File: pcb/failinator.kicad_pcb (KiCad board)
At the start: 2 copper layers, 200 x 124 mm, 82 parts, among them P1 CONN_01X04, P2 CONN_01X06, P3 CONN_01X06, P4 CONN_01X06, U1 74HC594, U2 RASPIPLUSHEADER, U3 LDS-CD16RI, U4 LDS-CD16RI, U5 74HC594

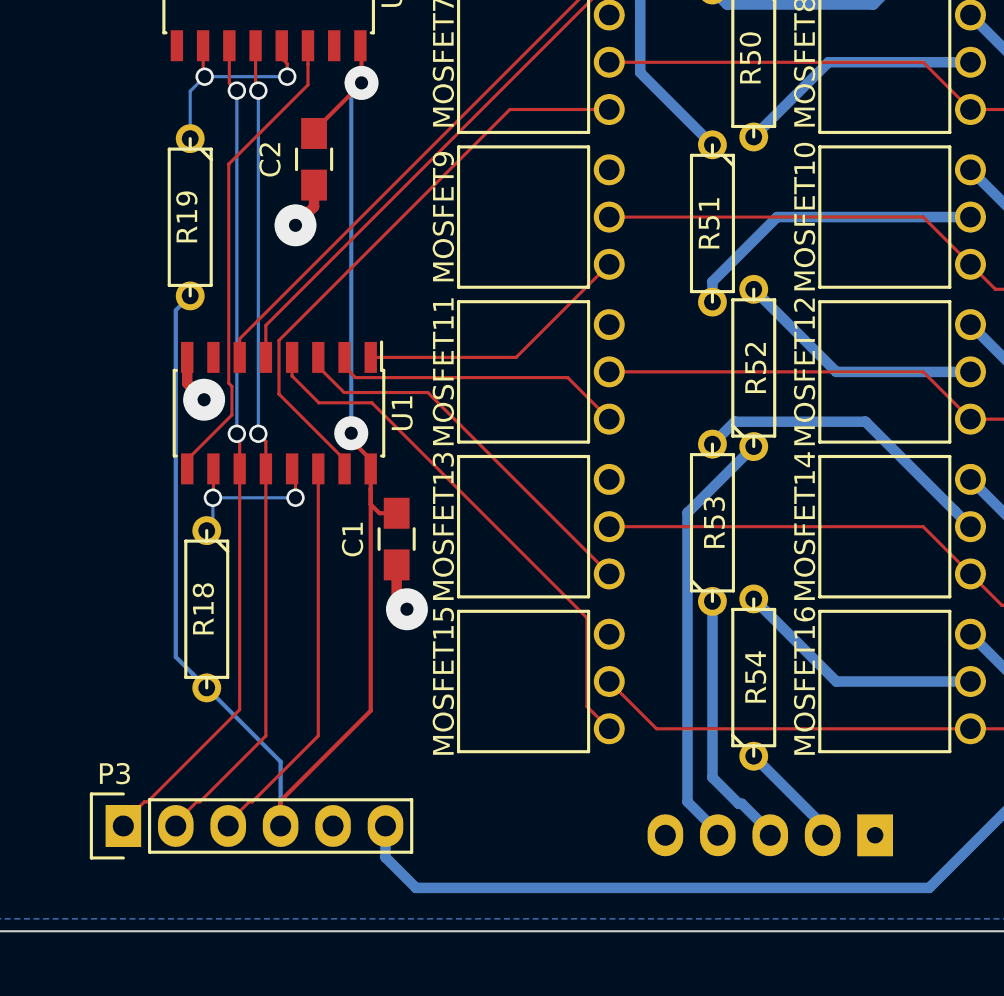
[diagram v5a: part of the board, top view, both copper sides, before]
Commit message: Place some grounds better so they are in the main copper pour
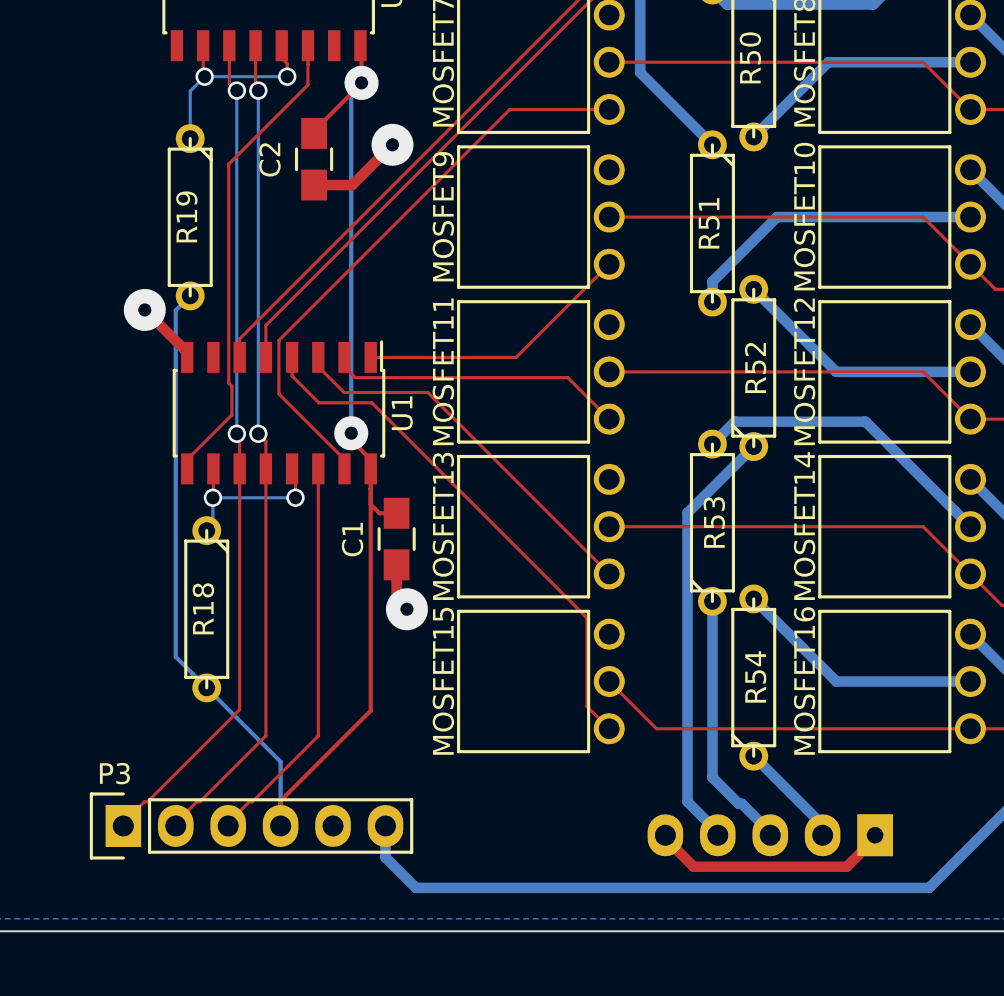
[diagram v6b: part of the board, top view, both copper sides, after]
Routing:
- net /DisplayDrivers/GND: track 9.09 -> 23.7 mm
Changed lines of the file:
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@@
     (thickness 1.6)
     (drawings 16)
-    (tracks 372)
+    (tracks 376)
     (zones 0)
     (modules 82)
@@
   (segment (start 125.5 96.5) (end 125.5 118.75) (width 0.508) (layer F.Cu) (net 37) (status 10))
   (segment (start 125.5 118.75) (end 124.25 120) (width 0.508) (layer F.Cu) (net 37) (status 20))
-  (segment (start 249.7 33.45) (end 249.7 34.5) (width 0.508) (layer F.Cu) (net 38))
-  (segment (start 249.7 34.5) (end 248.8 35.4) (width 0.508) (layer F.Cu) (net 38))
-  (via (at 248.8 35.4) (size 2.032) (drill 0.635) (layers F.Cu B.Cu) (net 38))
+  (segment (start 276.88 64.95) (end 276.88 65.1024) (width 0.508) (layer F.Cu) (net 38))
+  (segment (start 276.88 65.1024) (end 275.50839 66.47401) (width 0.508) (layer F.Cu) (net 38))
+  (segment (start 268.09161 66.47401) (end 266.72 65.1024) (width 0.508) (layer F.Cu) (net 38))
+  (segment (start 275.50839 66.47401) (end 268.09161 66.47401) (width 0.508) (layer F.Cu) (net 38))
+  (segment (start 266.72 65.1024) (end 266.72 64.95) (width 0.508) (layer F.Cu) (net 38))
+  (segment (start 249.7 33.45) (end 251.55 33.45) (width 0.508) (layer F.Cu) (net 38))
+  (segment (start 251.55 33.45) (end 253.5 31.5) (width 0.508) (layer F.Cu) (net 38))
+  (via (at 253.5 31.5) (size 2.032) (drill 0.635) (layers F.Cu B.Cu) (net 38))
+  (segment (start 243.555 41.8) (end 243.555 41.555) (width 0.508) (layer F.Cu) (net 38))
+  (segment (start 243.555 41.555) (end 241.5 39.5) (width 0.508) (layer F.Cu) (net 38))
+  (via (at 241.5 39.5) (size 2.032) (drill 0.635) (layers F.Cu B.Cu) (net 38))
   (segment (start 253.7 51.85) (end 253.7 53.5) (width 0.508) (layer F.Cu) (net 38))
   (segment (start 253.7 53.5) (end 254.2 54) (width 0.508) (layer F.Cu) (net 38))
   (via (at 254.2 54) (size 2.032) (drill 0.635) (layers F.Cu B.Cu) (net 38))
-  (segment (start 244.346901 43.849901) (end 244.373121 43.849901) (width 0.508) (layer F.Cu) (net 38))
-  (segment (start 243.555 43.058) (end 244.346901 43.849901) (width 0.508) (layer F.Cu) (net 38))
-  (segment (start 243.555 41.8) (end 243.555 43.058) (width 0.508) (layer F.Cu) (net 38))
-  (via (at 244.373121 43.849901) (size 2.032) (drill 0.635) (layers F.Cu B.Cu) (net 38))
   (segment (start 243.055 21.3) (end 243.055 22.805841) (width 0.508) (layer F.Cu) (net 38))
   (segment (start 243.055 22.805841) (end 243.410718 23.161559) (width 0.508) (layer F.Cu) (net 38))

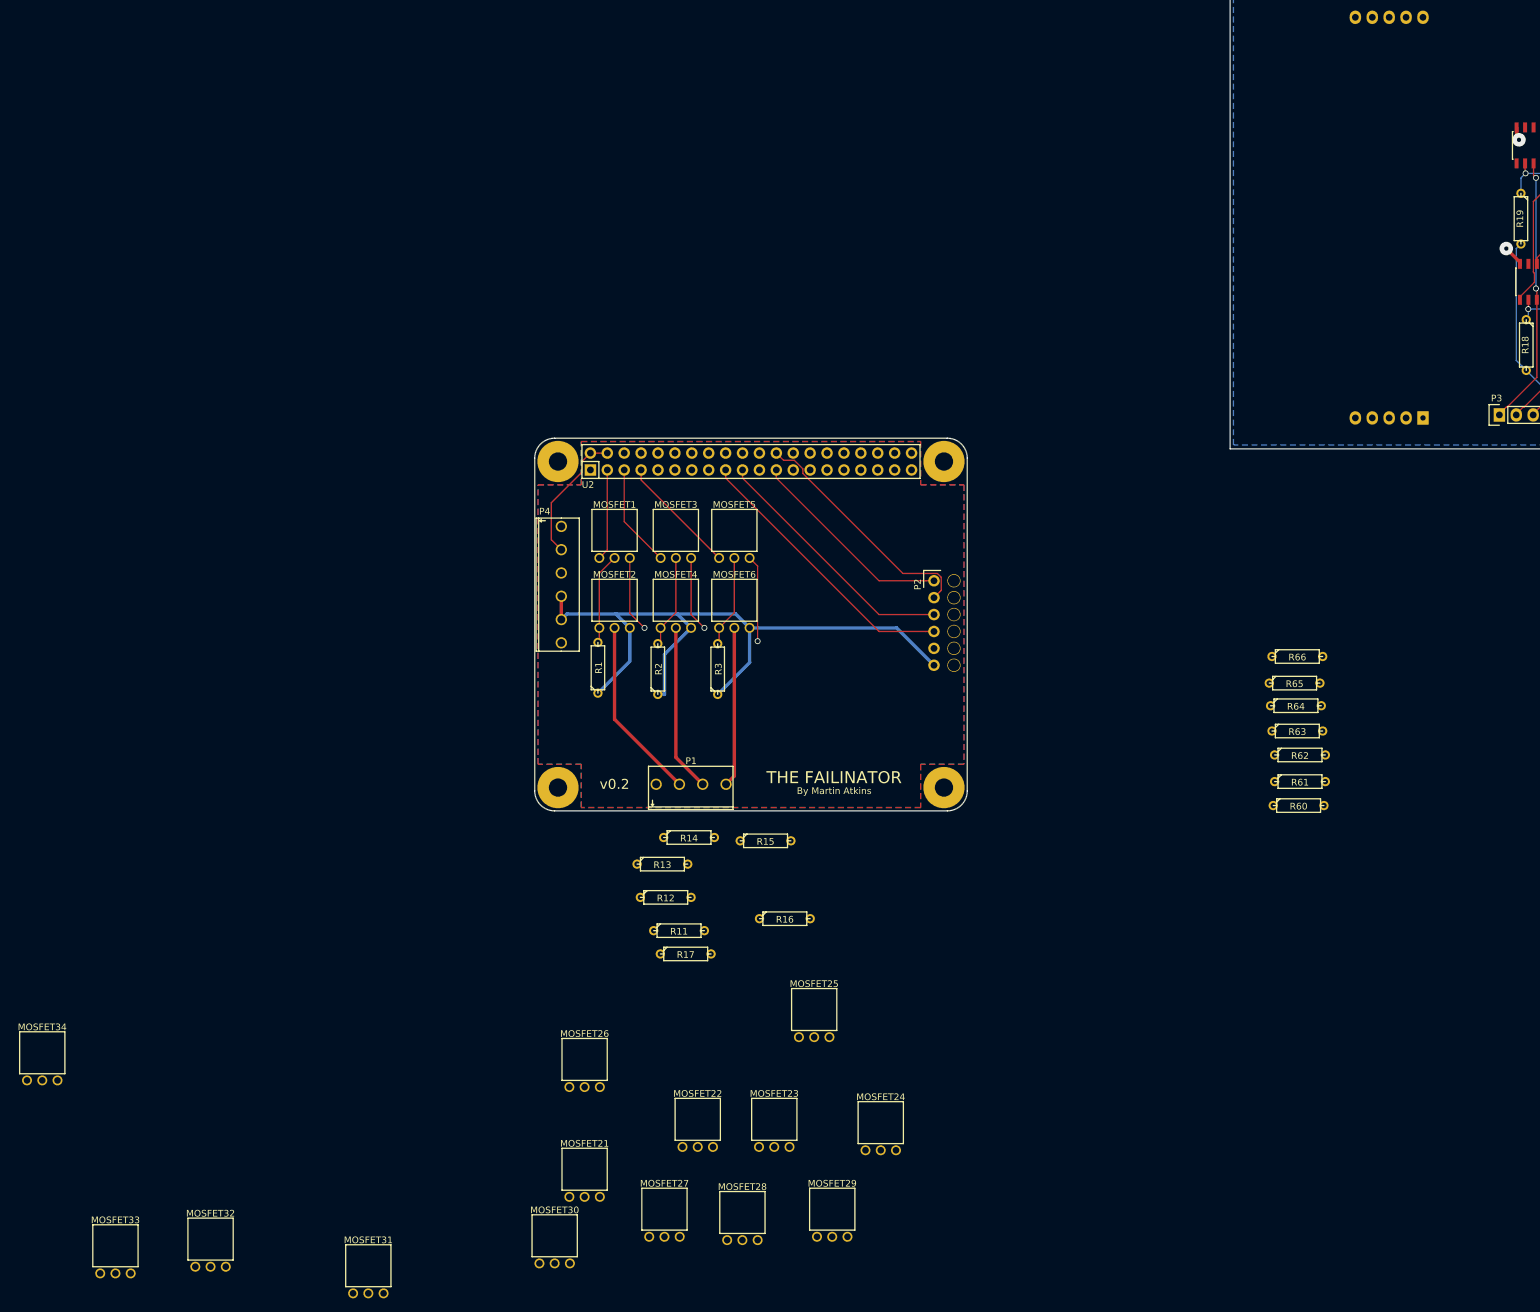
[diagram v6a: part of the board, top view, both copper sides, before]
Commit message: Placement of components for digit 1
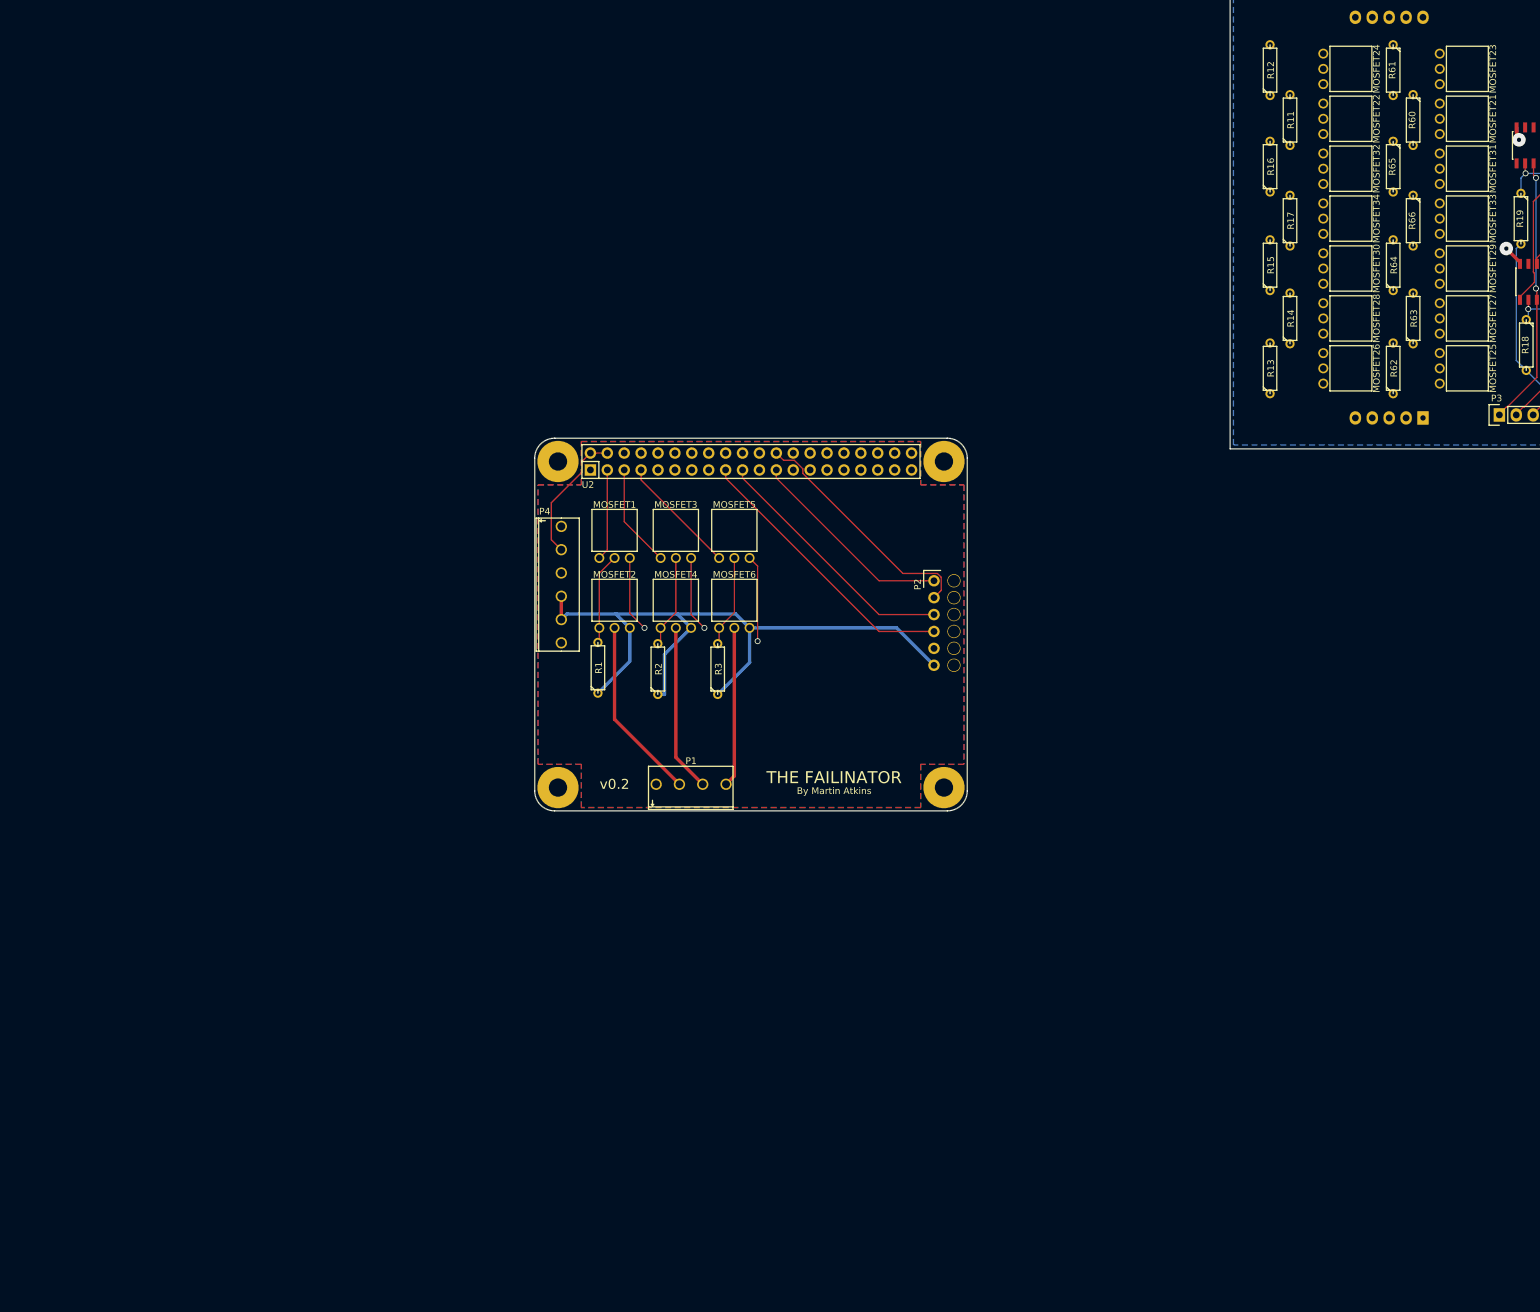
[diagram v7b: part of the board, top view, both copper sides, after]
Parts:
- moved MOSFET33 254.4 mm to (231.5, 35.0), turned to 270 degrees
- moved MOSFET32 234.9 mm to (214.0, 27.5), turned to 270 degrees
- moved MOSFET31 233.4 mm to (231.5, 27.5), turned to 270 degrees
- moved MOSFET34 232.0 mm to (214.0, 35.0), turned to 270 degrees
- moved MOSFET21 206.8 mm to (231.5, 20.0), turned to 270 degrees
- moved MOSFET23 190.4 mm to (231.5, 12.5), turned to 270 degrees
- moved MOSFET30 188.9 mm to (214.0, 42.5), turned to 270 degrees
- moved MOSFET22 180.8 mm to (214.0, 20.0), turned to 270 degrees
- moved MOSFET27 180.6 mm to (231.5, 50.0), turned to 270 degrees
- moved MOSFET24 175.6 mm to (214.0, 12.5), turned to 270 degrees
- moved MOSFET29 171.8 mm to (231.5, 42.5), turned to 270 degrees
- moved MOSFET28 163.7 mm to (214.0, 50.0), turned to 270 degrees
- moved MOSFET26 154.9 mm to (214.0, 57.5), turned to 270 degrees
- moved R12 153.9 mm to (206.0, 12.7), turned to 90 degrees
- moved R11 152.5 mm to (209.0, 20.2), turned to 90 degrees
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
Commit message: Digit 1 traces
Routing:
- net /DisplayDrivers/VIN: track 161.4 -> 331.7 mm
- net /DisplayDrivers/C1_L: track 0.00 -> 44.4 mm
- net /DisplayDrivers/D1_L: track 0.00 -> 35.9 mm
- net /DisplayDrivers/B1_L: track 0.00 -> 28.2 mm
- net /DisplayDrivers/G1_P: track 0.00 -> 27.8 mm
- net /DisplayDrivers/A1_L: track 0.00 -> 27.7 mm
- net /DisplayDrivers/E1_L: track 0.00 -> 27.4 mm
- net Net-(MOSFET29-Pad2): track 0.00 -> 27.3 mm
- net Net-(MOSFET31-Pad2): track 0.00 -> 27.2 mm
- net Net-(MOSFET25-Pad2): track 0.00 -> 27.1 mm
- net Net-(MOSFET23-Pad2): track 0.00 -> 27.0 mm
- net Net-(MOSFET27-Pad2): track 0.00 -> 24.1 mm
- net Net-(MOSFET21-Pad2): track 0.00 -> 24.0 mm
- net Net-(MOSFET33-Pad2): track 0.00 -> 23.9 mm
- net /DisplayDrivers/F1_P: track 0.00 -> 21.9 mm
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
